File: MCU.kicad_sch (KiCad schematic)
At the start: 30 parts, among them J5 Conn_01x12, Q5 MMBT3904, Q6 MMBT3904, SW1 SW_DPDT_x2, SW2 PTS647SN50SMTR2_LFS, SW3 PTS647SN50SMTR2_LFS, U4 CP2102N-Axx-xQFN28, U5 ESP32-C3-WROOM-02, U6 LIS3DH

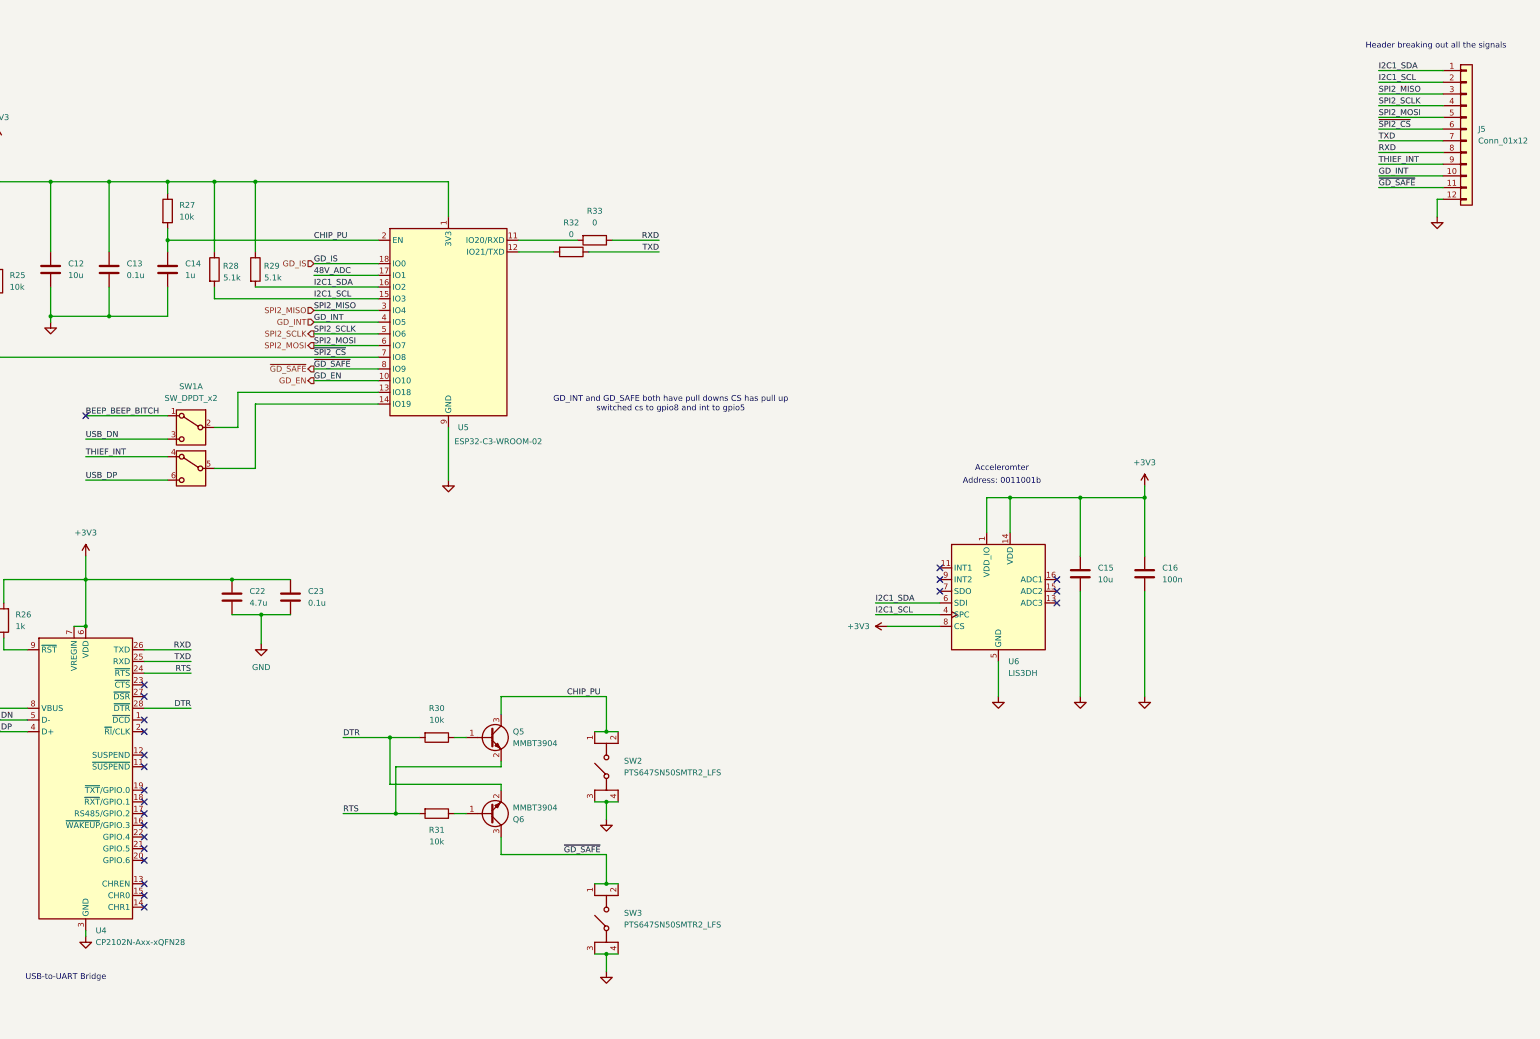
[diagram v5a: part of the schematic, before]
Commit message: Finished Routing and ran DRC. Will need final review of schematics and layout with Austin. Will also need to update BOM.
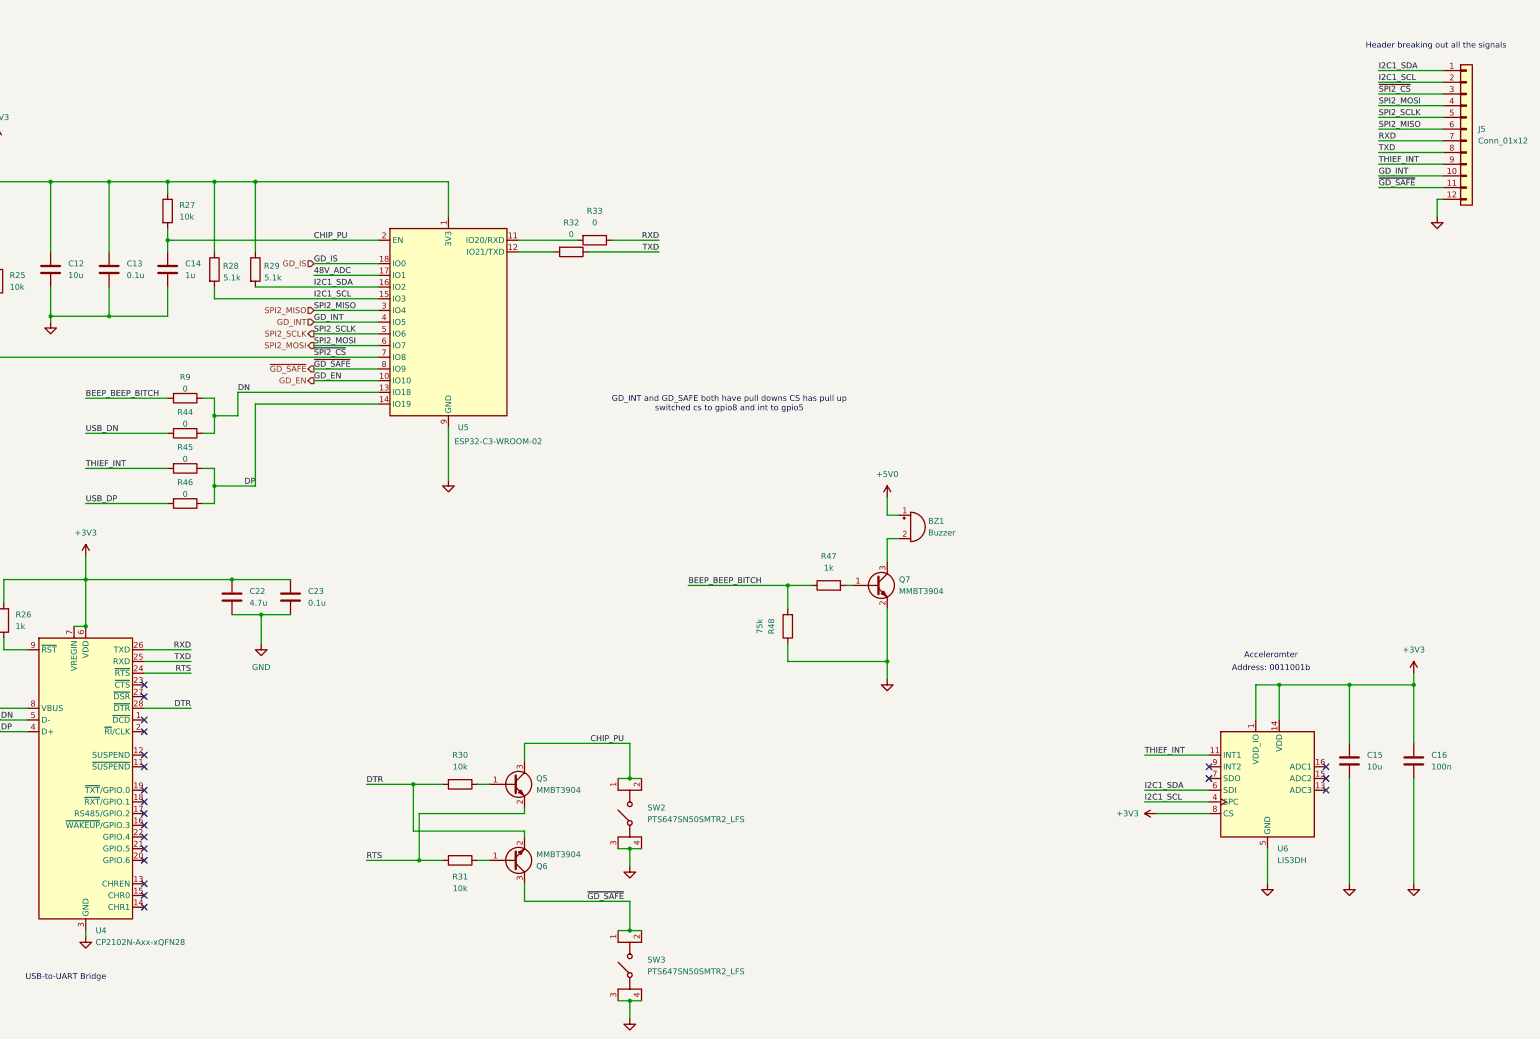
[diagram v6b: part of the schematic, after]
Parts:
- removed SW1: SW_DPDT_x2, Button_Switch_THT:SW_CK_JS202011CQN_DPDT_Straight, symbol Switch:SW_DPDT_x2
- added BZ1: Buzzer, custom_footprints:MagneticBuzzer_CT_1205C_SMT_TR, symbol Device:Buzzer
- added Q7: MMBT3904, Package_TO_SOT_SMD:SOT-23, symbol Transistor_BJT:MMBT3904
- added R44, R45, R46, R9: 0, Resistor_SMD:R_0603_1608Metric, symbol Device:R
- added R47: 1k, Resistor_SMD:R_0603_1608Metric, symbol Device:R
- added R48: 75k, Resistor_SMD:R_0603_1608Metric, symbol Device:R
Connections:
- net +5V0: now also BZ1.1 (+)
- net BEEP_BEEP_BITCH: now also R47.1, R48.2, R9.2
- net GND: now also Q7.2 (E), R48.1
- net RXD: now also J5.7 (Pin_7); no longer J5.8 (Pin_8)
- net SPI2_MISO: now also J5.6 (Pin_6); no longer J5.3 (Pin_3)
- net SPI2_MOSI: now also J5.4 (Pin_4); no longer J5.5 (Pin_5)
- net SPI2_SCLK: now also J5.5 (Pin_5); no longer J5.4 (Pin_4)
- net THIEF_INT: now also U6.11 (INT1), R45.2
- net TXD: now also J5.8 (Pin_8); no longer J5.7 (Pin_7)
- net USB_DN: now also R44.2
- net USB_DP: now also R46.2
- net ~{SPI2_CS}: now also J5.3 (Pin_3); no longer J5.6 (Pin_6)
- net DP: now reaches U5.14 (IO19)
- net DP: now also R45.1, R46.1
- net DN: now reaches U5.13 (IO18)
- net DN: now also R44.1, R9.1
- new net: BZ1.2 (-), Q7.3 (C)
- new net: Q7.1 (B), R47.2
- no-connect marks 23 -> 21
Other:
- moved on the sheet: C15, C16, Q5, Q6, R30, R31, SW2, SW3, U6

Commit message: add manufacturer, mpn, and package to bom
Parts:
- C11, C14: Manufacturer_Name (none) -> Taiyo Yuden; Manufacturer_Part_Number (none) -> TMK107B7105KA-T; Package (none) -> 603
- C12, C15: Manufacturer_Name (none) -> Taiyo Yuden; Manufacturer_Part_Number (none) -> LMK107BBJ106MALT; Package (none) -> 603
- C13, C23: Manufacturer_Name (none) -> YAGEO; Manufacturer_Part_Number (none) -> CC0603KRX7R7BB104; Package (none) -> 603
- C16: Manufacturer_Name (none) -> Samsung Electro-Mechanics; Manufacturer_Part_Number (none) -> CL10B104KC8NNNC; Package (none) -> 603
- C22: Manufacturer_Name (none) -> Samsung Electro-Mechanics; Manufacturer_Part_Number (none) -> CL10A475KP8NNNC; Package (none) -> 603
- Q5, Q6, Q7: Manufacturer_Name (none) -> Taiwan Semiconductor Corporation; Manufacturer_Part_Number (none) -> MMBT3904 RFG; Package (none) -> SOT-23
- R23: Manufacturer_Name (none) -> YAGEO; Manufacturer_Part_Number (none) -> RC0603FR-0722K1L; Package (none) -> 603
- R24: Manufacturer_Name (none) -> YAGEO; Manufacturer_Part_Number (none) -> RC0603FR-0747K5L; Package (none) -> 603
- R25, R27, R30, R31: Manufacturer_Name (none) -> YAGEO; Manufacturer_Part_Number (none) -> RC0603JR-0710KL; Package (none) -> 603
- R26, R47: Manufacturer_Name (none) -> YAGEO; Manufacturer_Part_Number (none) -> RC0603FR-071KL; Package (none) -> 603
- R28, R29: Manufacturer_Name (none) -> YAGEO; Manufacturer_Part_Number (none) -> RC0603FR-075K1L; Package (none) -> 603
- R34, R48: Manufacturer_Name (none) -> YAGEO; Manufacturer_Part_Number (none) -> AC0603FR-0775KL; Package (none) -> 603
- R35: Manufacturer_Name (none) -> KOA Speer Electronics, Inc.; Manufacturer_Part_Number (none) -> RN73H1JTTD3701B25; Package (none) -> 603
- SW2, SW3: Package (none) -> SMT 4P
- U4: Manufacturer_Name (none) -> Silicon Labs; Manufacturer_Part_Number (none) -> CP2102N-A02-GQFN28; Package (none) -> 28-QFN
- U5: Manufacturer_Name (none) -> Espressif Systems; Manufacturer_Part_Number (none) -> ESP32-C3-WROOM-02-H4; Package (none) -> SMT
- U6: Manufacturer_Name (none) -> STMicroelectronics; Manufacturer_Part_Number (none) -> LIS3DH; Package (none) -> LGA-16

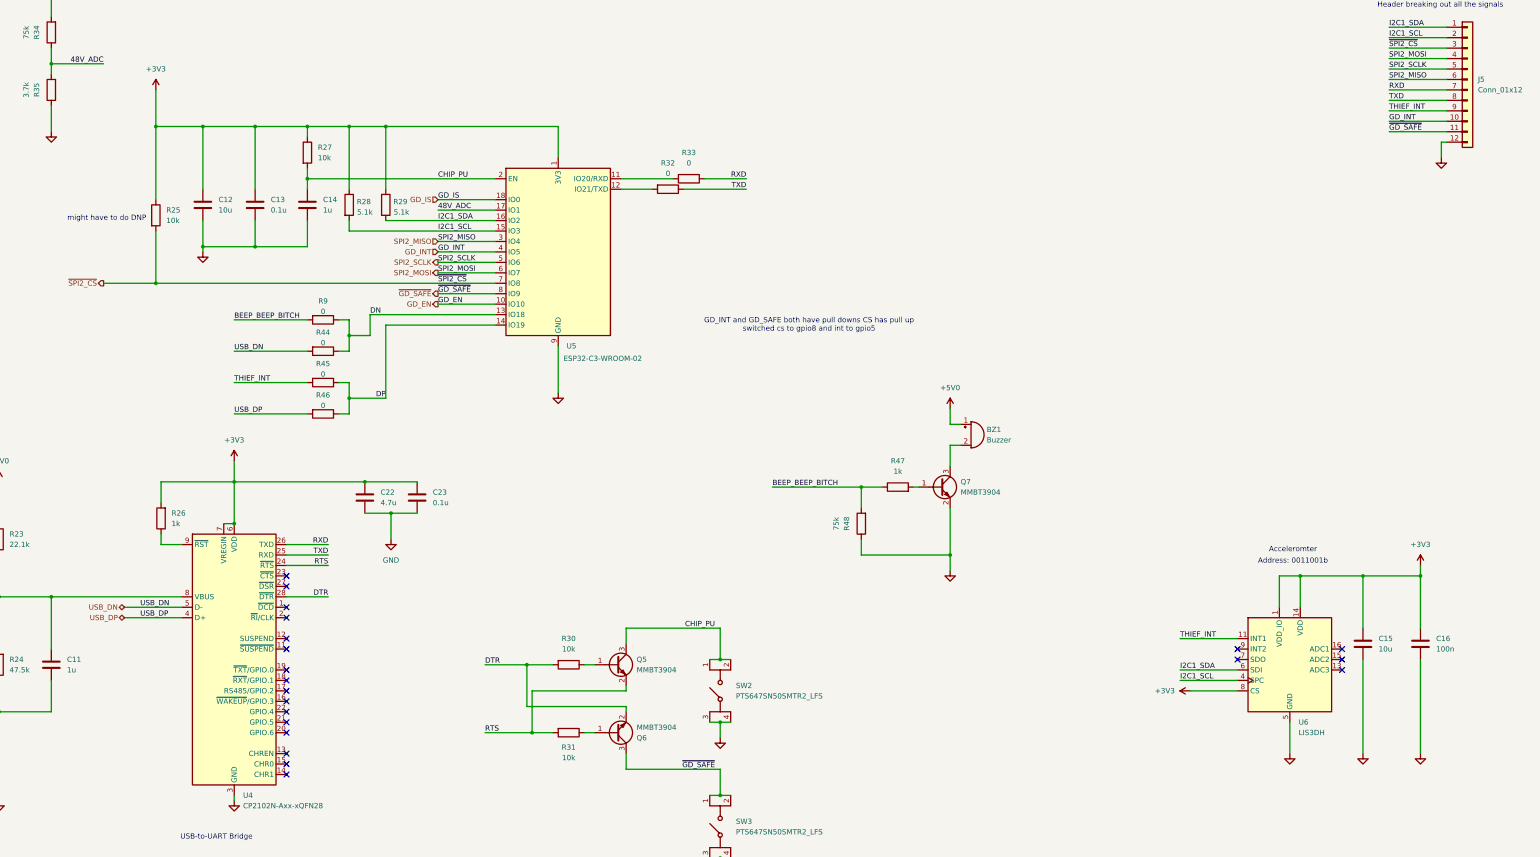
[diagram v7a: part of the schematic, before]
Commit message: Caught some issues and made final changes for manufacturing (#9)
Caught some issues and made final changes for manufacturing including correcting the imu and J2 footprints, updating the clearance rules we imported from pcbway (.09mm->0.1mm), and the addition of stitching capacitors for usb signal.
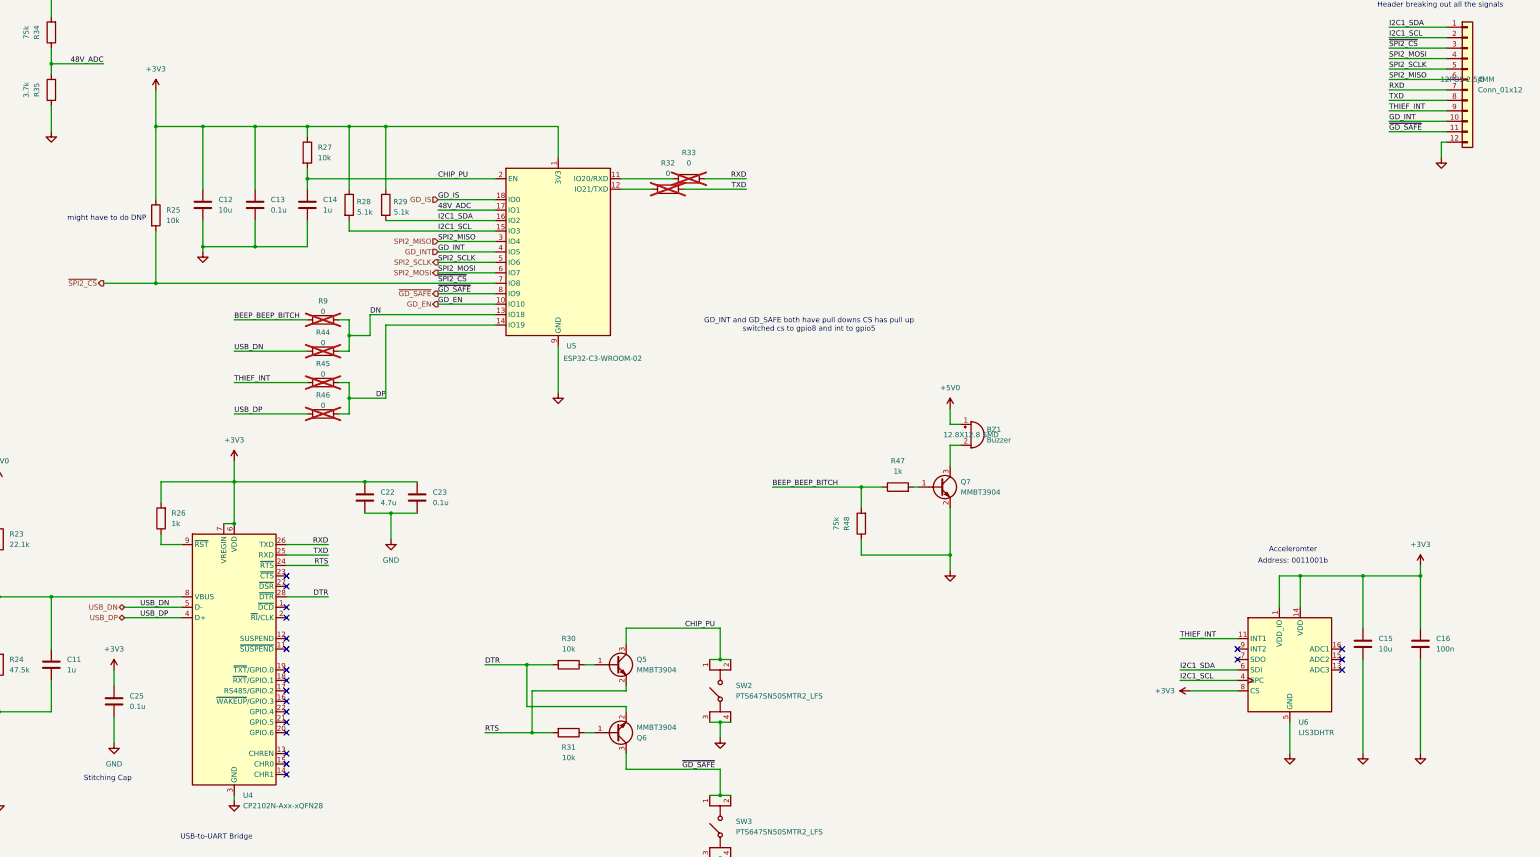
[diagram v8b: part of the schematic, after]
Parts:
- added C25: 0.1u, Capacitor_SMD:C_0603_1608Metric, symbol Device:C
- BZ1: Manufacturer_Name (none) -> Same Sky (Formerly CUI Devices); Manufacturer_Part_Number (none) -> CT-1205C-SMT-TR; Package (none) -> 12.8X12.8 SMD
- J5: Manufacturer_Name (none) -> Adam Tech; Manufacturer_Part_Number (none) -> PH1-12-UA; Package (none) -> 12POS 2.54MM
- R32, R33, R44, R45, R46, R9: footprint Resistor_SMD:R_0603_1608Metric -> Resistor_SMD:R_0201_0603Metric; now not fitted
- U6: value LIS3DH -> LIS3DHTR; footprint Package_LGA:LGA-16_3x3mm_P0.5mm_LayoutBorder3x5y -> custom_footprints:LGA-16_3x3mm_P0.5mm_LayoutBorder3x5y_2; Manufacturer_Part_Number LIS3DH -> LIS3DHTR; Package LGA-16 -> 16-LGA
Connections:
- net +3V3: now also C25.1
- net GND: now also C25.2
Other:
- note added: "Stitching Cap"
